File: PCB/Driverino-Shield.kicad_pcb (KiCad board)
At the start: 2 copper layers, 68.6 x 53.3 mm, 58 parts, among them P1 Power, P10 MOT, P11 HALL, P2 Analog, P3 Digital, P4 Digital, P5 CONN_01X01, P6 CONN_01X01, P7 CONN_01X01, P8 CONN_01X01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

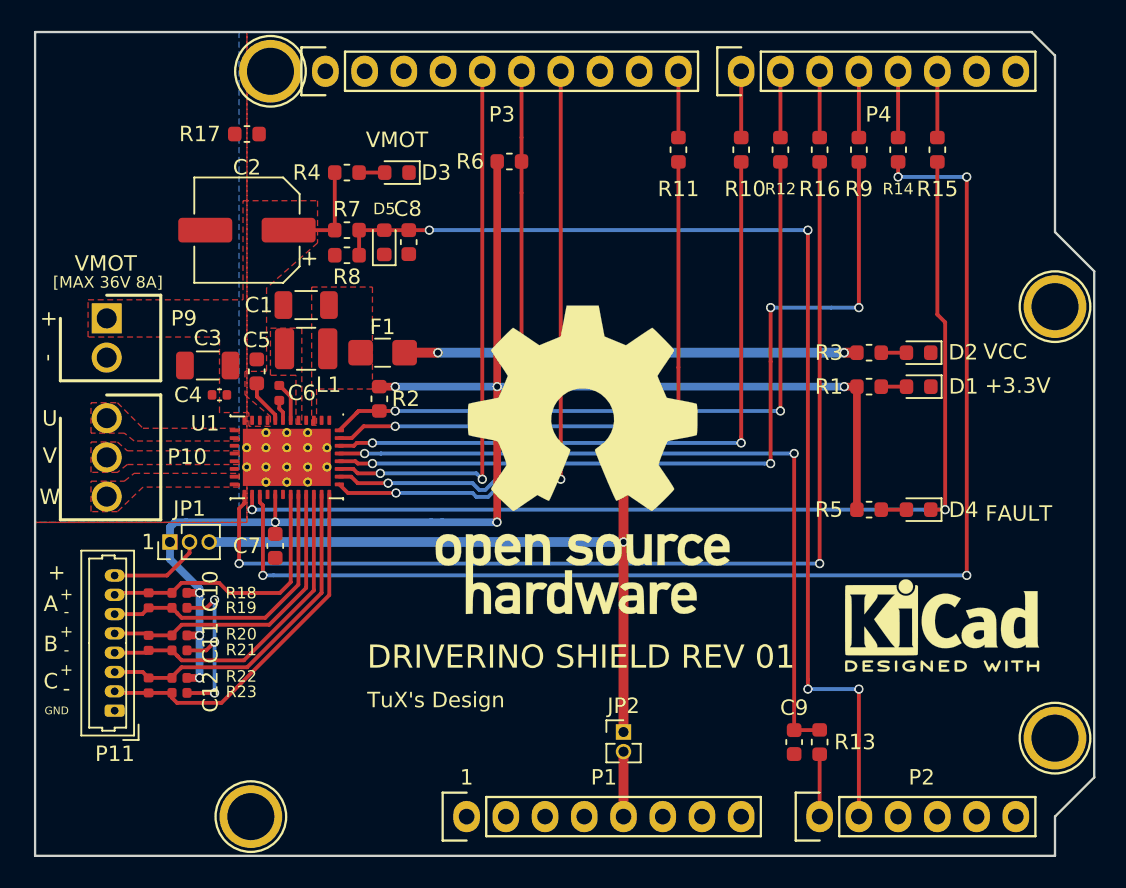
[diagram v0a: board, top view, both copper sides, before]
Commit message: Add teardrops
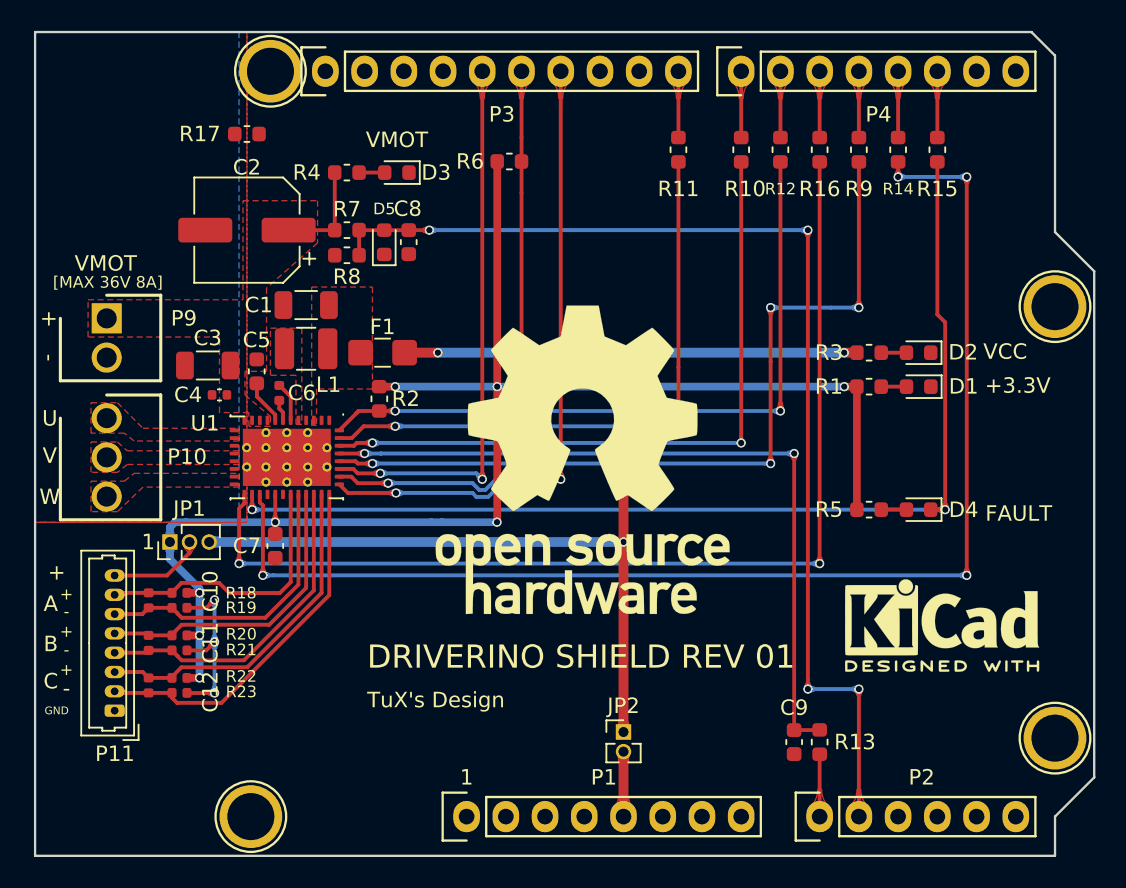
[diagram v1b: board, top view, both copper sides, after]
